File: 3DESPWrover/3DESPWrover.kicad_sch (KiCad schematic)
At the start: 21 parts

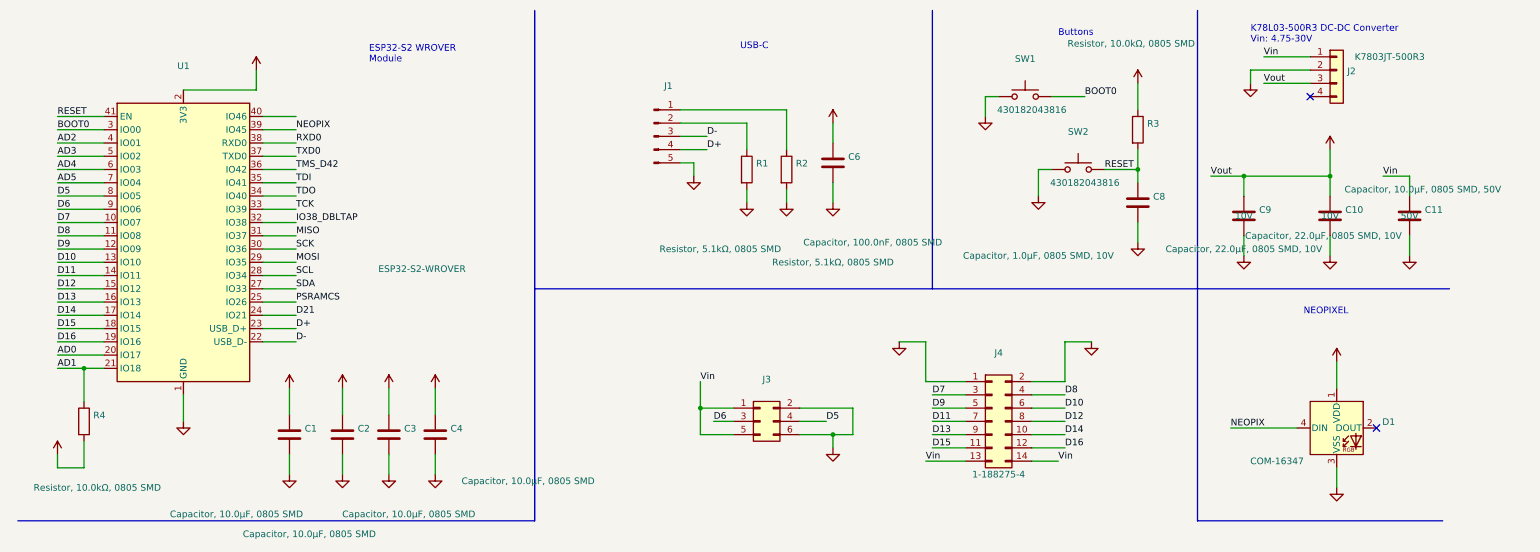
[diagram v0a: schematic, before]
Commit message: Added 0805 diode before 3.3 power source
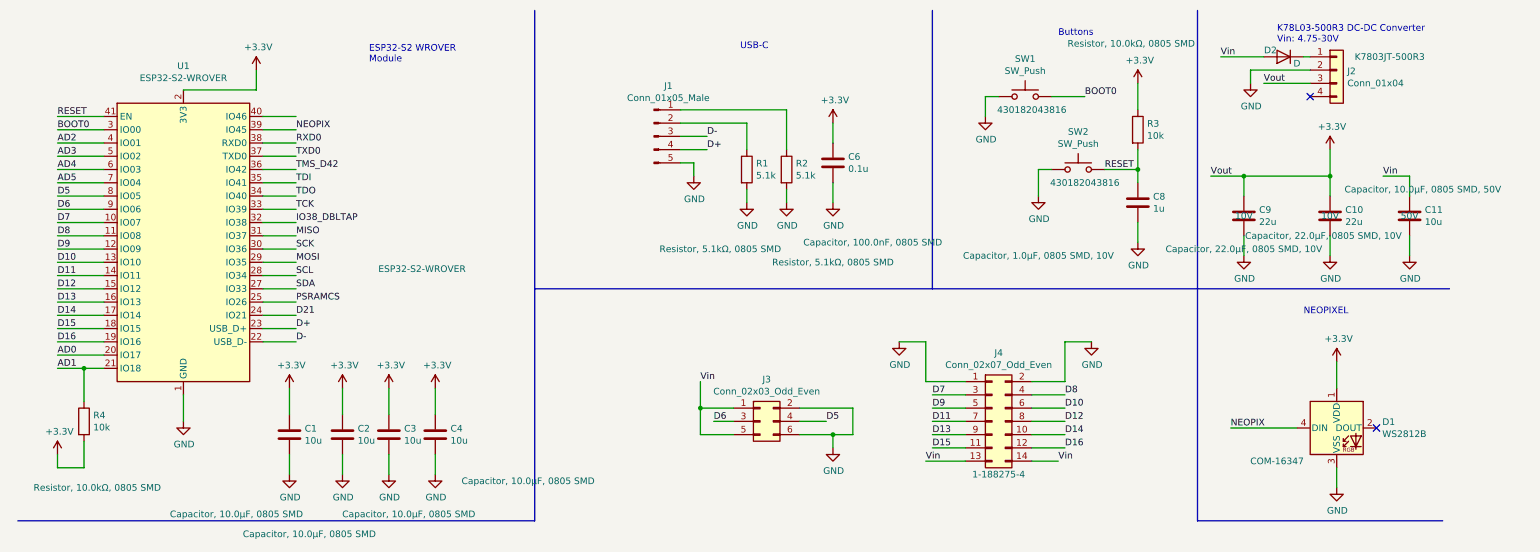
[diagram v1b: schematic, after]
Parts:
- added D2: D, Diode_SMD:D_0805_2012Metric_Pad1.15x1.40mm_HandSolder, symbol Device:D
- C1, C11, C2, C3, C4: value (none) -> 10u; footprint (none) -> Capacitor_SMD:C_0805_2012Metric_Pad1.18x1.45mm_HandSolder
- C10, C9: value (none) -> 22u; footprint (none) -> Capacitor_SMD:C_0805_2012Metric_Pad1.18x1.45mm_HandSolder
- C6: value (none) -> 0.1u; footprint (none) -> Capacitor_SMD:C_0805_2012Metric_Pad1.18x1.45mm_HandSolder
- C8: value (none) -> 1u; footprint (none) -> Capacitor_SMD:C_0805_2012Metric_Pad1.18x1.45mm_HandSolder
- D1: value (none) -> WS2812B; footprint (none) -> LED_SMD:LED_WS2812B_PLCC4_5.0x5.0mm_P3.2mm
- J1: value (none) -> Conn_01x05_Male; footprint (none) -> Connector_PinHeader_2.54mm:PinHeader_1x05_P2.54mm_Vertical
- J2: value (none) -> Conn_01x04; footprint (none) -> Custom:K7803JT-500R3-SMD
- J3: value (none) -> Conn_02x03_Odd_Even; footprint (none) -> Connector_PinHeader_2.54mm:PinHeader_2x03_P2.54mm_Vertical
- J4: value (none) -> Conn_02x07_Odd_Even; footprint (none) -> Custom:TE_Micromatch_2,54_14_SMD
- R1, R2: value (none) -> 5.1k; footprint (none) -> Resistor_SMD:R_0805_2012Metric_Pad1.20x1.40mm_HandSolder
- R3, R4: value (none) -> 10k; footprint (none) -> Resistor_SMD:R_0805_2012Metric_Pad1.20x1.40mm_HandSolder
- SW1, SW2: value (none) -> SW_Push; footprint (none) -> Button_Switch_SMD:SW_SPST_B3S-1000
- U1: value (none) -> ESP32-S2-WROVER; footprint (none) -> RF_Module:ESP32-S2-WROVER
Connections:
- net Vin: now also D2.2 (A); no longer J2.1 (Pin_1)
- new net: D2.1 (K), J2.1 (Pin_1)

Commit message: Updated esp32 footprint for 9 ground path underneath and correcting misalignments
Added protection resistors to digital pins

Moved decoupling capacitors closer to 3.3v line

Corrected legend positions and added indication of boot and reset buttons
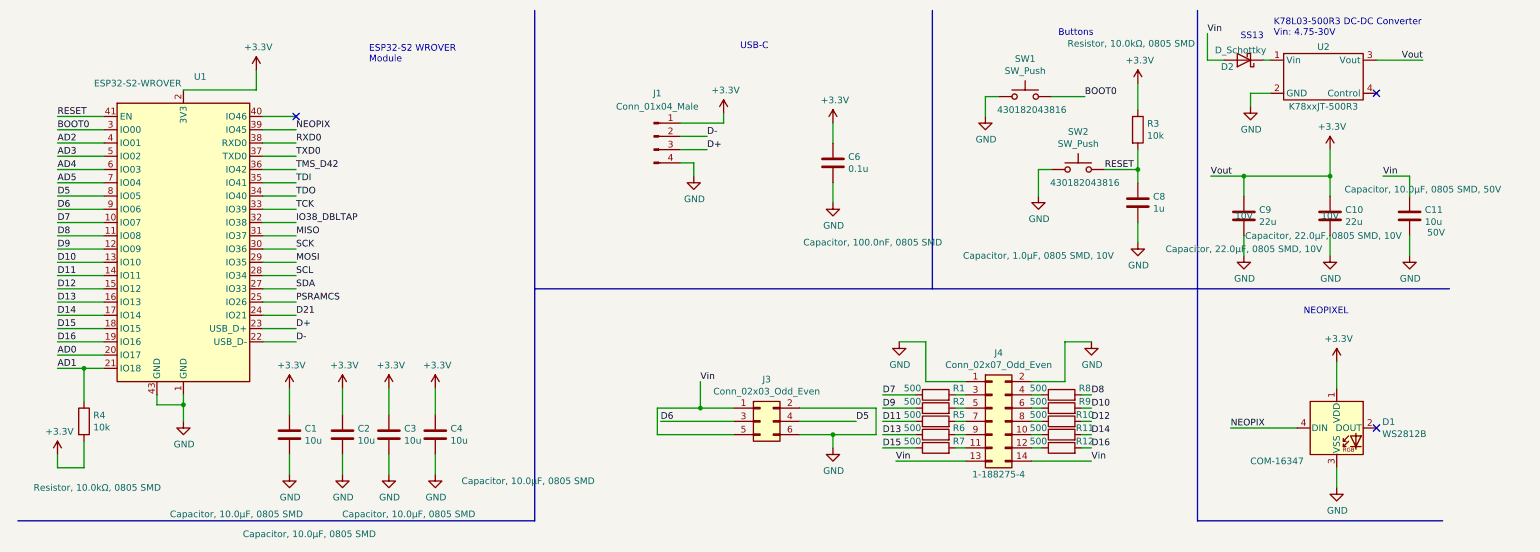
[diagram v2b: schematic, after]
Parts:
- removed D2: D, Diode_SMD:D_0805_2012Metric_Pad1.15x1.40mm_HandSolder, symbol Device:D
- removed J1: Conn_01x05_Male, Connector_PinHeader_2.54mm:PinHeader_1x05_P2.54mm_Vertical, symbol Connector:Conn_01x05_Male
- removed J2: Conn_01x04, Custom:K7803JT-500R3-SMD, symbol Connector_Generic:Conn_01x04
- removed U1: ESP32-S2-WROVER, RF_Module:ESP32-S2-WROVER, symbol RF_Module:ESP32-S2-WROVER
- added D2: D_Schottky, Diode_SMD:D_SMA, symbol Device:D_Schottky
- added J1: Conn_01x04_Male, Connector_PinHeader_2.54mm:PinHeader_1x04_P2.54mm_Vertical, symbol Connector:Conn_01x04_Male
- added R10, R11, R12, R5, R6, R7, R8, R9: 500, Resistor_SMD:R_0603_1608Metric_Pad0.98x0.95mm_HandSolder, symbol Device:R
- added U1: ESP32-S2-WROVER, Custom:ESP32-S2-WROVER, symbol Custom:ESP32-S2-WROVER
- added U2: K78xxJT-500R3, Custom:K7803JT-500R3-SMD, symbol Custom:K78xxJT-500R3
- R1, R2: value 5.1k -> 500; footprint Resistor_SMD:R_0805_2012Metric_Pad1.20x1.40mm_HandSolder -> Resistor_SMD:R_0603_1608Metric_Pad0.98x0.95mm_HandSolder; MPN Resistor, 5.1kΩ, 0805 SMD -> (none)
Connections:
- net +3V3: now also J1.1 (Pin_1), U1.2 (3V3), U2.3 (Vout)
- net AD0: now also U1.20 (IO17)
- net AD1: now also U1.21 (IO18)
- net AD2: now also U1.4 (IO01)
- net AD3: now also U1.5 (IO02)
- net AD4: now also U1.6 (IO03)
- net AD5: now also U1.7 (IO04)
- net BOOT0: now also U1.3 (IO00)
- net D+: now also J1.3 (Pin_3), U1.23 (USB_D+)
- net D-: now also J1.2 (Pin_2), U1.22 (USB_D-)
- net D10: now also R9.2, U1.13 (IO10); no longer J4.6 (Pin_6)
- net D11: now also R5.1, U1.14 (IO11); no longer J4.7 (Pin_7)
- net D12: now also R10.2, U1.15 (IO12); no longer J4.8 (Pin_8)
- net D13: now also R6.1, U1.16 (IO13); no longer J4.9 (Pin_9)
- net D14: now also R11.2, U1.17 (IO14); no longer J4.10 (Pin_10)
- net D15: now also R7.1, U1.18 (IO15); no longer J4.11 (Pin_11)
- net D16: now also R12.2, U1.19 (IO16); no longer J4.12 (Pin_12)
- net D21: now also U1.24 (IO21)
- net D5: now also U1.8 (IO05)
- net D6: now also U1.9 (IO06)
- net D7: now also R1.1, U1.10 (IO07); no longer J4.3 (Pin_3)
- net D8: now also R8.2, U1.11 (IO08); no longer J4.4 (Pin_4)
- net D9: now also R2.1, U1.12 (IO09); no longer J4.5 (Pin_5)
- net GND: now also J1.4 (Pin_4), U1.1 (GND), U1.26 (GND), U1.42 (GND), U1.43 (GND), U1.44 (GND), U1.45 (GND), U1.46 (GND), U1.47 (GND), U1.48 (GND), U1.49 (GND), U1.50 (GND), U1.51 (GND), U2.2 (GND); no longer R1.2, R2.2
- net IO38_DBLTAP: now also U1.32 (IO38)
- net MISO: now also U1.31 (IO37)
- net MOSI: now also U1.29 (IO35)
- net NEOPIX: now also U1.39 (IO45)
- net PSRAMCS: now also U1.25 (IO26)
- net RESET: now also U1.41 (EN)
- net RXD0: now also U1.38 (RXD0)
- net SCK: now also U1.30 (IO36)
- net SCL: now also U1.28 (IO34)
- net SDA: now also U1.27 (IO33)
- net TCK: now also U1.33 (IO39)
- net TDI: now also U1.35 (IO41)
- net TDO: now also U1.34 (IO40)
- net TMS_D42: now also U1.36 (IO42)
- net TXD0: now also U1.37 (TXD0)
- net Vin: now also D2.2 (A)
- new net: J4.10 (Pin_10), R11.1
- new net: J4.11 (Pin_11), R7.2
- new net: J4.12 (Pin_12), R12.1
- new net: J4.3 (Pin_3), R1.2
- new net: J4.4 (Pin_4), R8.1
- new net: J4.5 (Pin_5), R2.2
- new net: J4.6 (Pin_6), R9.1
- new net: J4.7 (Pin_7), R5.2
- new net: J4.8 (Pin_8), R10.1
- new net: J4.9 (Pin_9), R6.2
- new net: D2.1 (K), U2.1 (Vin)
- no-connect marks 2 -> 3
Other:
- note added: "SS13"
